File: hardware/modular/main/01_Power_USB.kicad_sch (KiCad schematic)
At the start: 15 parts, among them J1 TYPE-C-31-M-12, U1 TPD2EUSB30DRTR, U11 TUSB320LAIRWBR, U2 TPS62162DSGR, U20 TPD2E2U06DCKR

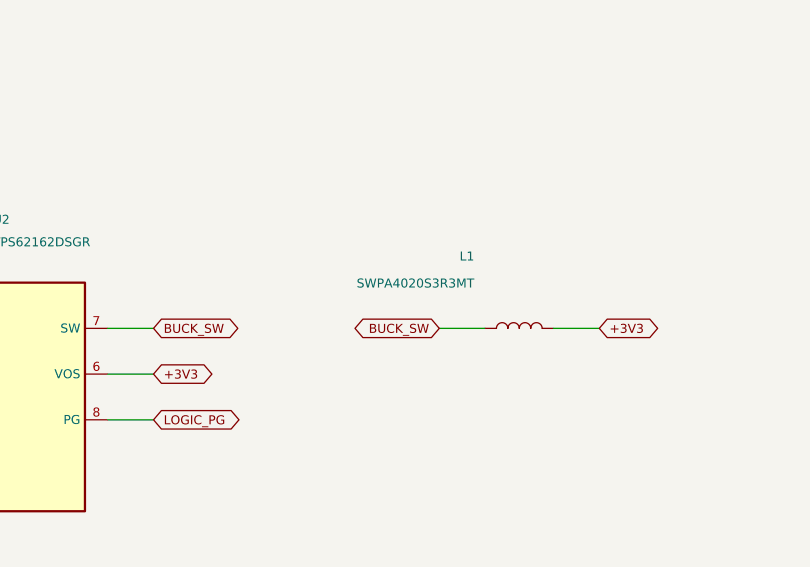
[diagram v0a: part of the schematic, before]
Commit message: Prepare wired Rev-A bench boards and submit manufacturing review
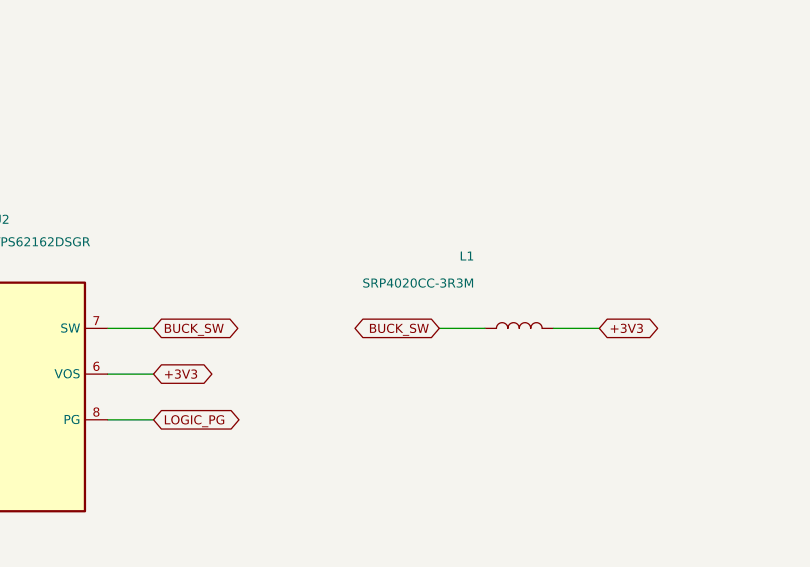
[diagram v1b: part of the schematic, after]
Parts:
- L1: value SWPA4020S3R3MT -> SRP4020CC-3R3M; footprint Inductor_SMD:L_Sunlord_SWPA4020S -> MagMouseModular:L_Bourns_SRP4020CC; Checked 2026-09-08 -> 2026-09-12; JLCPCB Part # C83424 -> (none); LCSC C83424 -> (none); MPN SWPA4020S3R3MT -> SRP4020CC-3R3M; Manufacturer Sunlord -> Bourns; Sourcing Status Catalog MPN verified 2026-09-08; stock and assembly quote m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 -> Bench replacement reviewed 2026-09-12; Mouser consumer purc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; Supplier URL https://www.lcsc.com/product-detail/C83424.html -> https://hr.mouser.com/ProductDetail/Bourns/SRP4020CC-3R3M
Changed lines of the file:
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@@
           (size 1.0 1.0))
         (justify left)))
-    (property "Value" "SWPA4020S3R3MT"
+    (property "Value" "SRP4020CC-3R3M"
       (at 165.18 185.5 90)
       (effects
@@
           (size 1.0 1.0))
         (justify left)))
-    (property "Footprint" "Inductor_SMD:L_Sunlord_SWPA4020S"
+    (property "Footprint" "MagMouseModular:L_Bourns_SRP4020CC"
       (at 170.18 190.5 0)
       (hide yes)
@@
           (size 1.0 1.0))
         (justify left)))
-    (property "Datasheet" "https://atta.szlcsc.com/upload/public/pdf/source/20210916/AC798BA7E846B7D0B6818F45CD84DB0B.pdf"
+    (property "Datasheet" "https://www.bourns.com/docs/product-datasheets/srp4020cc.pdf"
       (at 170.18 190.5 0)
       (hide yes)
@@
           (size 1.0 1.0))
         (justify left)))
-    (property "Manufacturer" "Sunlord"
+    (property "Manufacturer" "Bourns"
       (at 170.18 190.5 0)
       (hide yes)
@@
           (size 1.0 1.0))
         (justify left)))
-    (property "MPN" "SWPA4020S3R3MT"
+    (property "MPN" "SRP4020CC-3R3M"
       (at 170.18 190.5 0)
       (hide yes)
@@
           (size 1.0 1.0))
         (justify left)))
-    (property "LCSC" "C83424"
+    (property "LCSC" ""
       (at 170.18 190.5 0)
       (hide yes)
@@
           (size 1.0 1.0))
         (justify left)))
-    (property "JLCPCB Part #" "C83424"
+    (property "JLCPCB Part #" ""
       (at 170.18 190.5 0)
       (hide yes)
@@
           (size 1.0 1.0))
         (justify left)))
-    (property "Sourcing Status" "Catalog MPN verified 2026-09-08; stock and assembly quote must be refreshed"
+    (property "Sourcing Status" "Bench replacement reviewed 2026-09-12; Mouser consumer purchase; stock not reserved"
       (at 170.18 190.5 0)
       (hide yes)
@@
           (size 1.0 1.0))
         (justify left)))
-    (property "Checked" "2026-09-08"
+    (property "Checked" "2026-09-12"
       (at 170.18 190.5 0)
       (hide yes)
@@
           (size 1.0 1.0))
         (justify left)))
-    (property "Supplier URL" "https://www.lcsc.com/product-detail/C83424.html"
+    (property "Supplier URL" "https://hr.mouser.com/ProductDetail/Bourns/SRP4020CC-3R3M"
       (at 170.18 190.5 0)
       (hide yes)
